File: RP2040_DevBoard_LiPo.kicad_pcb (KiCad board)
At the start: 2 copper layers, 38 x 50 mm, 36 parts, among them J1 USB_C_Receptacle_USB2.0, J2 Conn_01x18, J3 Conn_01x18, SW1 SW_Push, SW2 SW_Push, U1 W25Q128JVS, U2 USBLC6-2SC6, U3 RP2040, U4 XC6206PxxxMR, Y1 Crystal_GND23

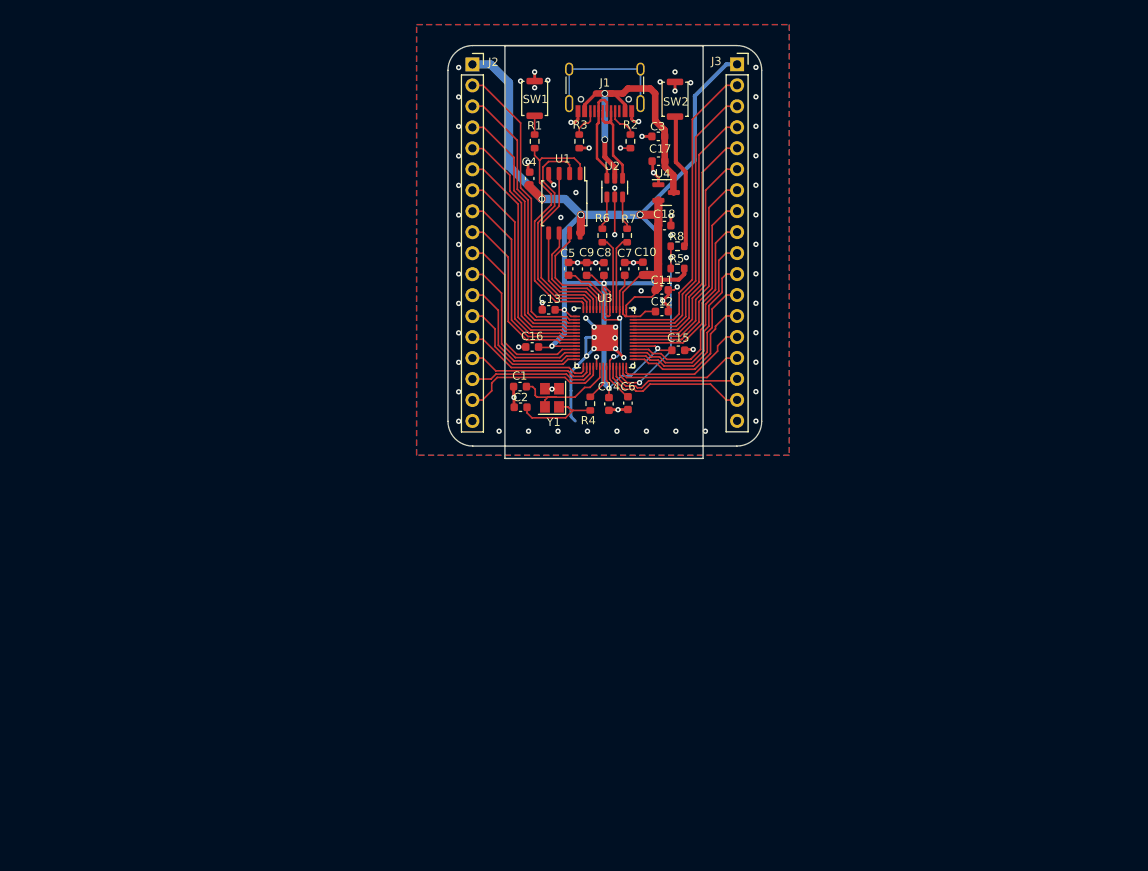
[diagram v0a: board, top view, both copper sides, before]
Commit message: added missing 3v3 arrow, changed some footprints
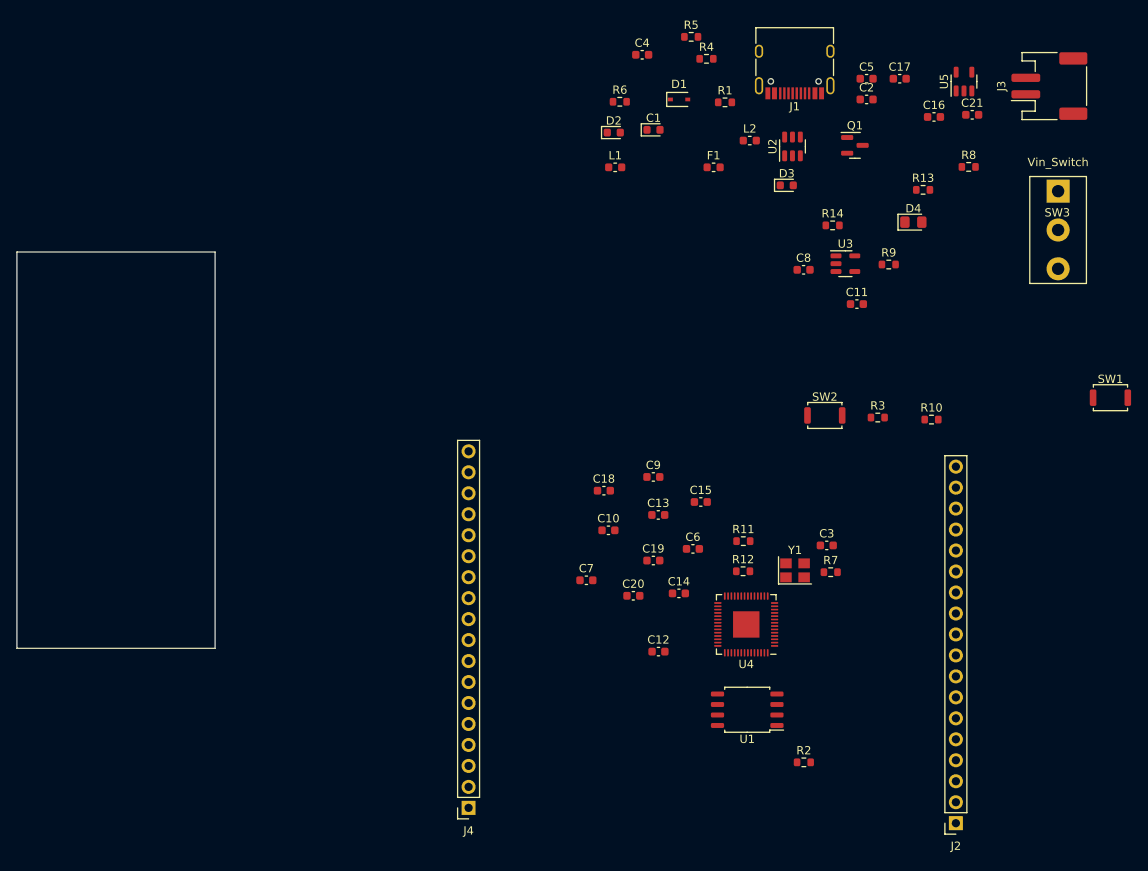
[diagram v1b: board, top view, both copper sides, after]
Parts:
- added C19: 1uF, Capacitor_SMD:C_0603_1608Metric, F.Cu at (145.1, 82.4)
- added C20: 1uF, Capacitor_SMD:C_0603_1608Metric, F.Cu at (142.7, 86.6)
- added C21: 4u7, Capacitor_SMD:C_0603_1608Metric, F.Cu at (183.7, 28.4)
- added D1: BSD3C051V, Diode_SMD:D_SOD-323, F.Cu at (148.2, 26.5)
- added D2: LED, LED_SMD:LED_0603_1608Metric, F.Cu at (140.3, 30.5)
- added D3: D_Schottky, Diode_SMD:D_0603_1608Metric, F.Cu at (161.2, 36.9)
- added D4: LED, LED_SMD:LED_0805_2012Metric_Pad1.15x1.40mm_HandSolder, F.Cu at (176.6, 41.4)
- added F1: 750 mA, Fuse:Fuse_0603_1608Metric, F.Cu at (152.4, 34.7)
- added J4: Conn_01x18, Connector_PinSocket_2.54mm:PinSocket_1x18_P2.54mm_Vertical, F.Cu at (122.7, 112.3)
- added L1: BLM15PX121SN1D, Inductor_SMD:L_0603_1608Metric, F.Cu at (140.5, 34.7)
- added L2: BLM15PX121SN1D, Inductor_SMD:L_0603_1608Metric, F.Cu at (156.8, 31.5)
- added Q1: DMP2045U, Package_TO_SOT_SMD:SOT-23, F.Cu at (169.5, 32.1)
- added R10: 1k, Resistor_SMD:R_0603_1608Metric, F.Cu at (178.8, 65.3)
- added R11: 27, Resistor_SMD:R_0603_1608Metric, F.Cu at (156.0, 80.0)
- added R12: 27, Resistor_SMD:R_0603_1608Metric, F.Cu at (155.9, 83.7)
- added R13: 470, Resistor_SMD:R_0603_1608Metric, F.Cu at (177.7, 37.5)
- added R14: 2k, Resistor_SMD:R_0603_1608Metric, F.Cu at (166.8, 41.8)
- added R9: 10k, Resistor_SMD:R_0603_1608Metric, F.Cu at (173.6, 46.5)
- added SW3: Vin_Switch, Buggy_Footprints:switch123, F.Cu at (194.1, 37.6)
- added U5: MCP73831-2-OT, Package_TO_SOT_SMD:SOT-23-5, F.Cu at (182.7, 24.4)
- C1: value 22pF -> 100 nF; footprint Capacitor_SMD:C_0603_1608Metric -> Diode_SMD:D_0603_1608Metric
- C11, C8: value 1uF -> 1u
- C16: value 1uF -> 4u7
- C3: value 10uF -> 22pF
- C4: value 1uF -> 10uF
- J3: value Conn_01x18 -> Battery; footprint Connector_PinSocket_2.54mm:PinSocket_1x18_P2.54mm_Vertical -> Connector_JST:JST_PH_S2B-PH-SM4-TB_1x02-1MP_P2.00mm_Horizontal
- R1: value 1k -> 1 MOhm
- R2, R3: value 5k1 -> 1k
- R4, R5: value 1k -> 5k1
- R6: value 27 -> 470
- R7: value 27 -> 1k
- R8: value 1k -> 10k
- U3: value RP2040 -> SOT23-5 200mA 3.3V; footprint Package_DFN_QFN:QFN-56-1EP_7x7mm_P0.4mm_EP3.2x3.2mm -> Package_TO_SOT_SMD:SOT-23-5
- U4: value XC6206PxxxMR -> RP2040; footprint Package_TO_SOT_SMD:SOT-23 -> Package_DFN_QFN:QFN-56-1EP_7x7mm_P0.4mm_EP3.2x3.2mm
- moved J2 109.0 mm to (181.7, 114.2), turned to 180 degrees
- moved SW1 78.6 mm to (200.4, 62.6), turned to 0 degrees
- moved R2 78.1 mm to (163.3, 106.8), turned to 0 degrees
- moved U1 65.2 mm to (156.4, 100.4), turned to 180 degrees
- moved C2 56.1 mm to (170.9, 26.5), turned to 0 degrees
- moved C16 56.1 mm to (179.1, 28.6)
- moved C3 53.6 mm to (166.1, 80.5)
- moved U4 53.2 mm to (156.3, 90.1), turned to 180 degrees
- moved R3 49.3 mm to (172.3, 65.0), turned to 0 degrees
- moved R7 47.6 mm to (166.6, 83.8), turned to 0 degrees
- moved R4 44.1 mm to (151.5, 21.6), turned to 0 degrees
- moved C5 42.8 mm to (170.9, 24.0), turned to 0 degrees
- moved SW2 42.4 mm to (165.8, 64.8), turned to 0 degrees
- moved C12 41.2 mm to (145.7, 93.4), turned to 0 degrees
- moved C7 38.0 mm to (137.0, 84.8), turned to 0 degrees
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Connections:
- C1 pad 1: XIN -> GNDPWR
- C1 pad 2: GND -> Earth
- C16 pad 2: +3V3 -> +5V
- C17 pad 2: +5V -> +3V3
- C2 pad 1: /CrysOut -> XIN
- C3 pad 1: GND -> Net-(C3-Pad1)
- C3 pad 2: +5V -> GND
- C4 pad 2: +3V3 -> +5V
- C5 pad 2: +1V1 -> +3V3
- C8 pad 1: GND -> /VSRC
- C8 pad 2: +3V3 -> GND
- C9 pad 2: +3V3 -> +1V1
- J1 pad A1: GND -> GNDPWR
- J1 pad A12: GND -> GNDPWR
- J1 pad A4: +5V -> VBUS
- J1 pad A9: +5V -> VBUS
- J1 pad B1: GND -> GNDPWR
- J1 pad B12: GND -> GNDPWR
- J1 pad B4: +5V -> VBUS
- J1 pad B9: +5V -> VBUS
- J1 pad S1: unconnected-(J1-PadS1) -> Earth
- J3 pad 1: +3V3 -> VBAT
- J3 pad 2: /GPIO29 -> GND
- R1 pad 1: /BOOT -> Earth
- R1 pad 2: QSPI_SS -> GNDPWR
- R2 pad 1: GND -> /BOOT
- R2 pad 2: /CC1 -> QSPI_SS
- R3 pad 1: /CC2 -> /RESET
- R3 pad 2: GND -> RUN
- R4 pad 1: /CrysOut -> GND
- R4 pad 2: XOUT -> /CC1
- R5 pad 1: RUN -> /CC2
- R5 pad 2: +3V3 -> GND
- R6 pad 1: USB_DP -> Net-(D2-Pad2)
- R6 pad 2: /DP -> +5V
- R7 pad 1: USB_DN -> Net-(C3-Pad1)
- R7 pad 2: /DN -> XOUT
- R8 pad 1: /RESET -> GND
- R8 pad 2: RUN -> +5V
- U3 pad 1: +3V3 -> /VSRC
- U3 pad 2: /GPIO0 -> GND
- U3 pad 3: /GPIO1 -> /ENABLE
- U3 pad 4: /GPIO2 -> unconnected-(U3-Pad4)
- U3 pad 5: /GPIO3 -> +3V3
- U4 pad 1: GND -> +3V3
- U4 pad 2: +3V3 -> /GPIO0
- U4 pad 3: +5V -> /GPIO1
- Y1 pad 1: /CrysOut -> Net-(C3-Pad1)
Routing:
- net +3V3: track 184.9 -> 0.00 mm, vias 8 -> 0
- net GND: track 66.5 -> 0.00 mm, vias 83 -> 0
- net /GPIO29: track 37.2 -> 0.00 mm
- net +5V: track 37.1 -> 0.00 mm, vias 2 -> 0
- net /GPIO0: track 37.0 -> 0.00 mm
- net /GPIO28: track 35.2 -> 0.00 mm
- net /GPIO1: track 34.9 -> 0.00 mm
- net /GPIO27: track 33.1 -> 0.00 mm
- net /GPIO2: track 33.0 -> 0.00 mm
- net QSPI_SS: track 32.0 -> 0.00 mm
- net /GPIO26: track 31.1 -> 0.00 mm
- net /GPIO3: track 30.8 -> 0.00 mm
- net /GPIO25: track 29.0 -> 0.00 mm
- net /GPIO4: track 28.8 -> 0.00 mm
- net QSPI_SD1: track 27.7 -> 0.00 mm
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- removed copper zone on B.Cu, net GND
- removed copper zone on F.Cu, net GND
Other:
- board size 38 x 50 mm -> 24 x 48 mm
